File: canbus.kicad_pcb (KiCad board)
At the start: 2 copper layers, 34.5 x 37.6 mm, 15 parts, among them J1 Conn_01x08, J2 RJ45, J3 RJ45, U1 MCP2515-E/SO, U2 MCP2562-H/SN, Y1 Crystal_GND24

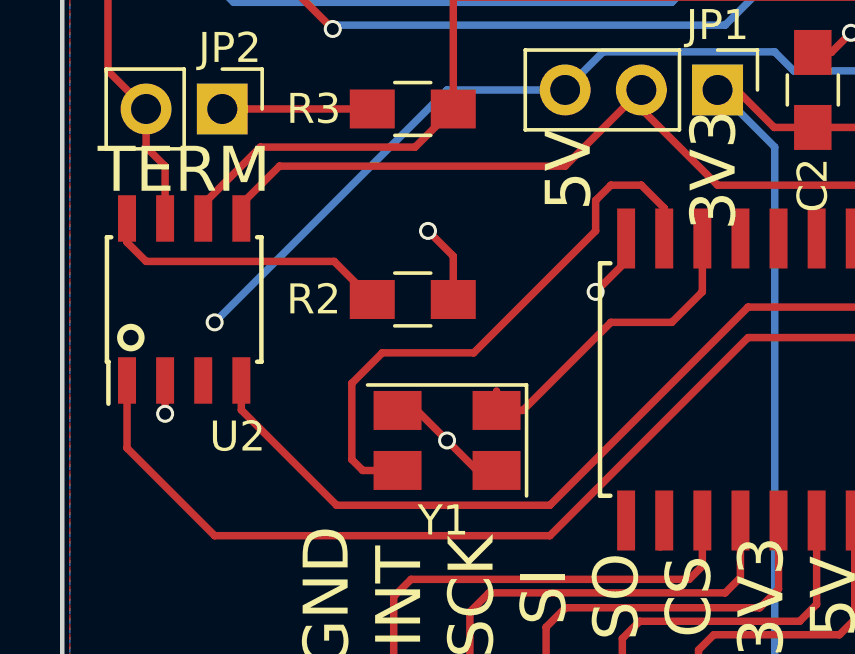
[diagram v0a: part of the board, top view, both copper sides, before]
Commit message: Modified layout to include capacitors for oscillator
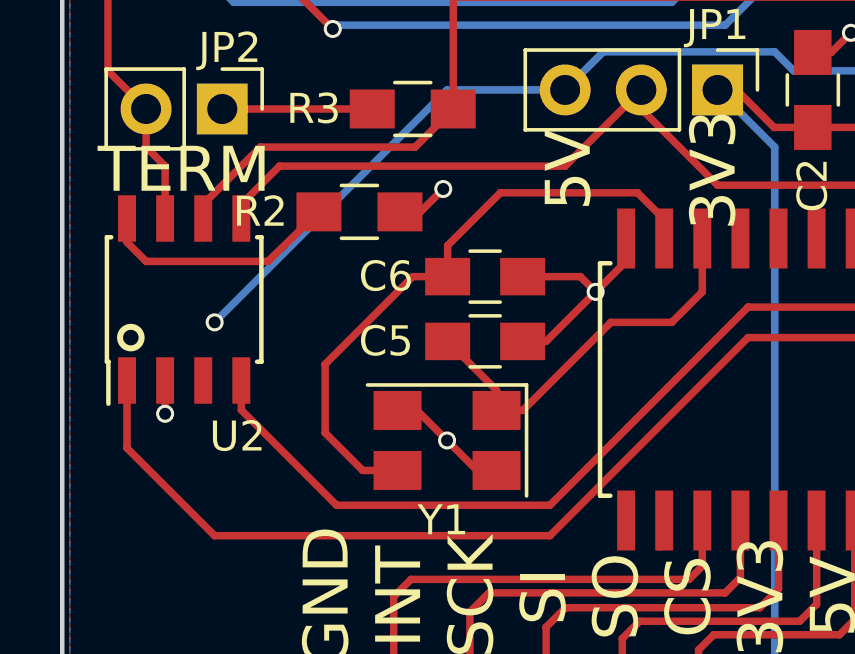
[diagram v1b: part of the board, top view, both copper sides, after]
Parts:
- added C5: 22uf, Capacitors_SMD:C_0805_HandSoldering, F.Cu at (152.3, 104.3)
- added C6: 22uf, Capacitors_SMD:C_0805_HandSoldering, F.Cu at (152.3, 102.1)
- moved R2 3.42 mm to (148.1, 99.9)
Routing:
- net GND: track 19.1 -> 24.0 mm
- net Net-(C5-Pad1): track 10.8 -> 13.8 mm
- net Net-(R2-Pad1): track 9.76 -> 8.13 mm
- net Net-(C6-Pad1): track 19.5 -> 20.6 mm

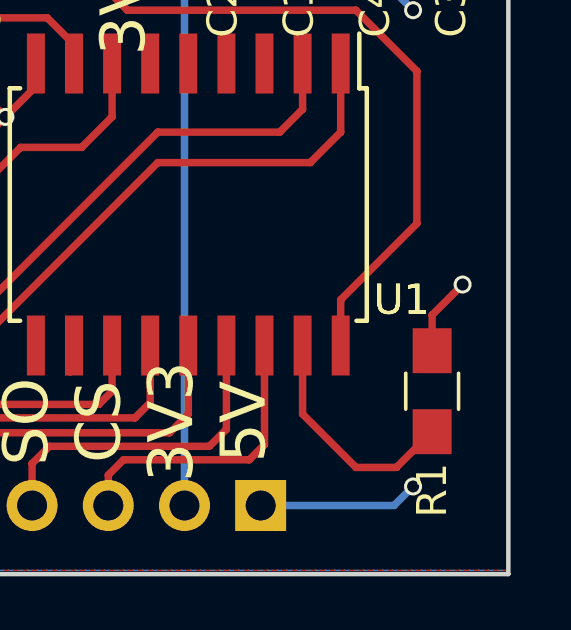
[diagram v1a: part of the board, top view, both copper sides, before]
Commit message: Fixed MCP2515 Reset pullup
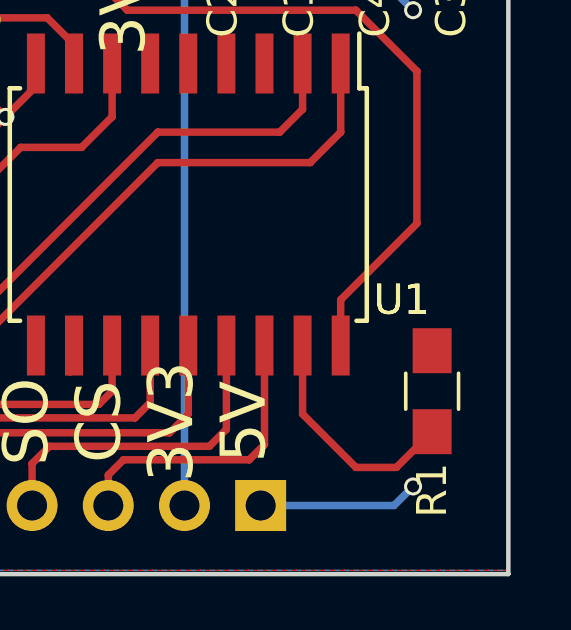
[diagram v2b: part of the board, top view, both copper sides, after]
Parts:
- R1: value 1k -> 10k
- R2: value 100k -> 10k
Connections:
- R1 pad 2: GND -> +5V
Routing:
- net GND: track 24.0 -> 21.4 mm, vias 7 -> 6
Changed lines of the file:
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@@
     (thickness 1.6)
     (drawings 9)
-    (tracks 174)
+    (tracks 171)
     (zones 0)
     (modules 17)
@@
       (effects (font (size 1 1) (thickness 0.15)))
     )
-    (fp_text value 1k (at 0 -1.27 90) (layer F.Fab)
+    (fp_text value 10k (at 0 -1.27 90) (layer F.Fab)
       (effects (font (size 1 1) (thickness 0.15)))
     )
@@
       (net 18 "Net-(R1-Pad1)"))
     (pad 2 smd rect (at 1.35 0 90) (size 1.5 1.3) (layers F.Cu F.Paste F.Mask)
-      (net 2 GND))
+      (net 3 +5V))
     (model ${KISYS3DMOD}/Resistors_SMD.3dshapes/R_0805.wrl
       (at (xyz 0 0 0))
@@
       (effects (font (size 1 1) (thickness 0.15)))
     )
-    (fp_text value 100k (at 0 -1.27) (layer F.Fab)
+    (fp_text value 10k (at 0 -1.27) (layer F.Fab)
       (effects (font (size 1 1) (thickness 0.15)))
     )
@@
   (segment (start 161.905 97.135) (end 163.195 97.135) (width 0.25) (layer F.Cu) (net 1))
   (segment (start 165.735 97.135) (end 163.195 97.135) (width 0.25) (layer F.Cu) (net 1))
-  (segment (start 153.523 102.108) (end 155.448 102.108) (width 0.25) (layer F.Cu) (net 2) (status 400000))
+  (segment (start 153.523 102.108) (end 155.448 102.108) (width 0.25) (layer F.Cu) (net 2))
   (via (at 155.956 102.616) (size 0.6) (drill 0.4) (layers F.Cu B.Cu) (net 2))
   (segment (start 155.448 102.108) (end 155.956 102.616) (width 0.25) (layer F.Cu) (net 2))
-  (segment (start 153.523 104.267) (end 154.305 104.267) (width 0.25) (layer F.Cu) (net 2) (status 400000))
+  (segment (start 153.523 104.267) (end 154.305 104.267) (width 0.25) (layer F.Cu) (net 2))
   (segment (start 155.956 102.616) (end 156.972 101.6) (width 0.25) (layer F.Cu) (net 2))
   (segment (start 154.305 104.267) (end 155.956 102.616) (width 0.25) (layer F.Cu) (net 2))
@@
   (via (at 150.876 99.187) (size 0.6) (drill 0.4) (layers F.Cu B.Cu) (net 2))
   (segment (start 156.972 100.964) (end 156.972 101.6) (width 0.25) (layer F.Cu) (net 2))
-  (segment (start 170.18 110.41) (end 170.18 109.22) (width 0.25) (layer F.Cu) (net 2))
-  (via (at 171.196 108.204) (size 0.6) (drill 0.4) (layers F.Cu B.Cu) (net 2))
-  (segment (start 170.18 109.22) (end 171.196 108.204) (width 0.25) (layer F.Cu) (net 2))
   (segment (start 170.815 94.635) (end 170.2 94.635) (width 0.25) (layer F.Cu) (net 2))
   (segment (start 170.2 94.635) (end 169.545 93.98) (width 0.25) (layer F.Cu) (net 2))
@@
   (segment (start 161.036 103.124) (end 165.1 103.124) (width 0.25) (layer F.Cu) (net 21))
   (segment (start 158.115 110.745) (end 158.115 111.125) (width 0.25) (layer F.Cu) (net 26))
-  (segment (start 152.653 106.569) (end 152.653 105.897) (width 0.25) (layer F.Cu) (net 28) (status 400000))
-  (segment (start 152.653 105.897) (end 151.023 104.267) (width 0.25) (layer F.Cu) (net 28) (status 800000))
+  (segment (start 152.653 106.569) (end 152.653 105.897) (width 0.25) (layer F.Cu) (net 28))
+  (segment (start 152.653 105.897) (end 151.023 104.267) (width 0.25) (layer F.Cu) (net 28))
   (segment (start 152.653 106.569) (end 153.527 106.569) (width 0.25) (layer F.Cu) (net 28))
   (segment (start 153.527 106.569) (end 156.464 103.632) (width 0.25) (layer F.Cu) (net 28))
@@
   (segment (start 158.496 103.632) (end 159.512 102.616) (width 0.25) (layer F.Cu) (net 28))
   (segment (start 159.512 102.616) (end 159.512 100.964) (width 0.25) (layer F.Cu) (net 28))
-  (segment (start 151.023 102.108) (end 151.023 101.072) (width 0.25) (layer F.Cu) (net 29) (status 400000))
-  (segment (start 157.353 99.314) (end 158.242 100.203) (width 0.25) (layer F.Cu) (net 29) (status 800000))
+  (segment (start 151.023 102.108) (end 151.023 101.072) (width 0.25) (layer F.Cu) (net 29))
+  (segment (start 157.353 99.314) (end 158.242 100.203) (width 0.25) (layer F.Cu) (net 29))
   (segment (start 152.781 99.314) (end 157.353 99.314) (width 0.25) (layer F.Cu) (net 29))
   (segment (start 151.023 101.072) (end 152.781 99.314) (width 0.25) (layer F.Cu) (net 29))
-  (segment (start 158.242 100.203) (end 158.242 100.837) (width 0.25) (layer F.Cu) (net 29) (status C00000))
-  (segment (start 151.023 102.108) (end 149.86 102.108) (width 0.25) (layer F.Cu) (net 29) (status 400000))
-  (segment (start 148.193 108.569) (end 149.353 108.569) (width 0.25) (layer F.Cu) (net 29) (status 800000))
+  (segment (start 158.242 100.203) (end 158.242 100.837) (width 0.25) (layer F.Cu) (net 29))
+  (segment (start 151.023 102.108) (end 149.86 102.108) (width 0.25) (layer F.Cu) (net 29))
+  (segment (start 148.193 108.569) (end 149.353 108.569) (width 0.25) (layer F.Cu) (net 29))
   (segment (start 146.939 107.315) (end 148.193 108.569) (width 0.25) (layer F.Cu) (net 29))
   (segment (start 146.939 105.029) (end 146.939 107.315) (width 0.25) (layer F.Cu) (net 29))
